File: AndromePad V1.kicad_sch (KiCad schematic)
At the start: 0 parts

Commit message: finished default hackpad tutorial
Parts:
- added D1, D2: SK6812MINI, LED_SMD:LED_SK6812MINI_PLCC4_3.5x3.5mm_P1.75mm, symbol LED:SK6812MINI
- added SW1, SW2, SW3, SW4: SW_Push, Button_Switch_Keyboard:SW_Cherry_MX_1.00u_PCB, symbol Switch:SW_Push
- added U1: XIAO-RP2040-DIP, OPL_Footprints:XIAO-RP2040-DIP, symbol OPL:XIAO-RP2040-DIP
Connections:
- new net: D1.3 (DIN), U1.5 (GPIO6/SDA)
- new net: D1.1 (DOUT), D2.3 (DIN)
- new net +5V: D1.4 (VDD), D2.4 (VDD), U1.14 (VBUS)
- new net GND: D1.2 (VSS), D2.2 (VSS), SW1.1, SW2.1, SW3.1, SW4.1, U1.13 (GND)
- new net Pin 10: SW3.2, U1.10 (GPIO4/MISO)
- new net Pin 11: SW1.2, U1.11 (GPIO3/MOSI)
- new net Pin 8: SW4.2, U1.8 (GPIO1/RX)
- new net Pin 9: SW2.2, U1.9 (GPIO2/SCK)
- no-connect marks 0 -> 8
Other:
- company: (none) -> DwayneR Engineering
- title: (none) -> Andromepad V1

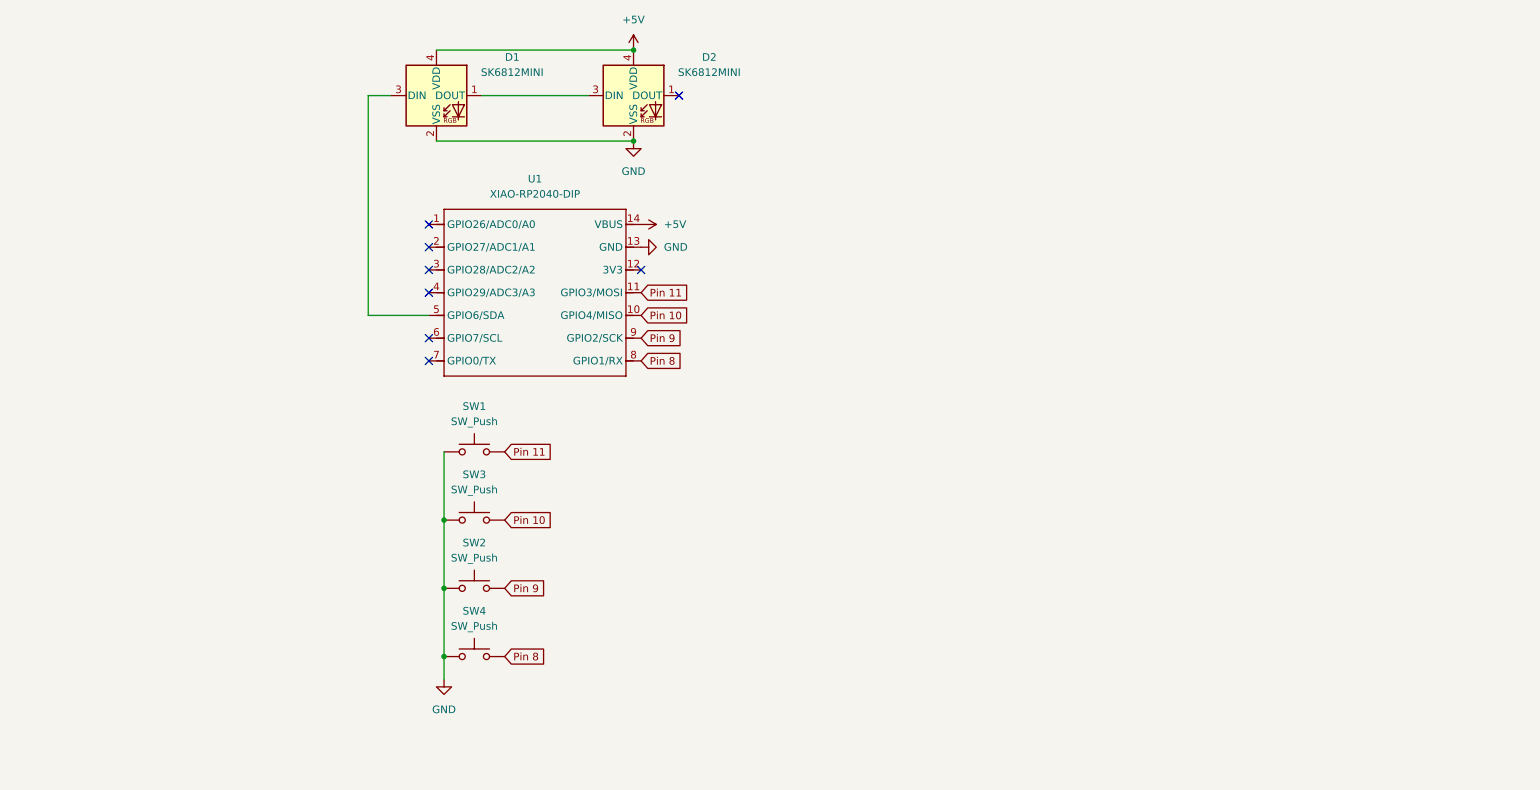
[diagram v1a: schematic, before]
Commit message: completed schematic, still have to work out errors and assign proper footprints
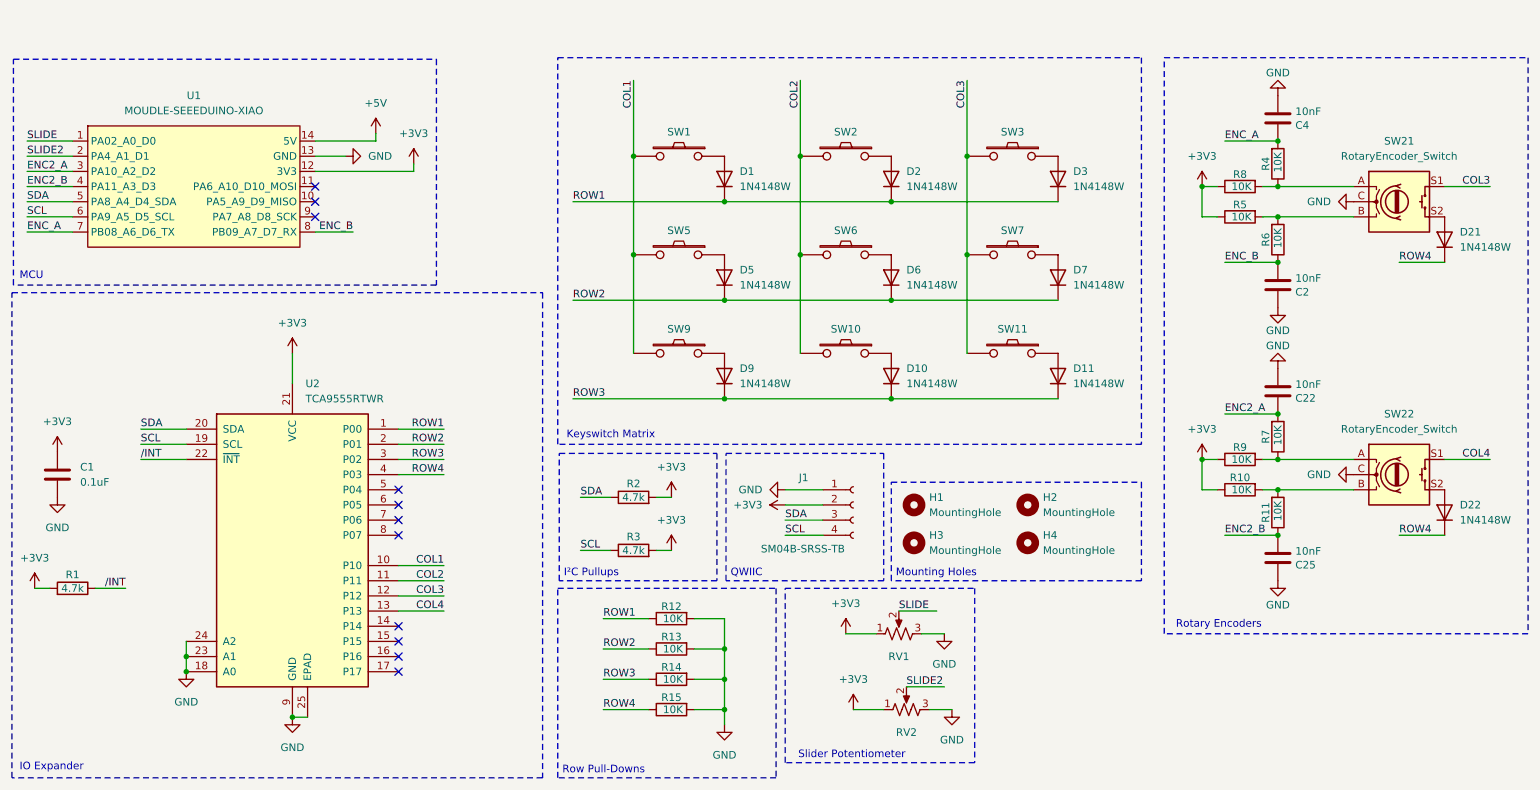
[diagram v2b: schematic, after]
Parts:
- removed D1, D2: SK6812MINI, LED_SMD:LED_SK6812MINI_PLCC4_3.5x3.5mm_P1.75mm, symbol LED:SK6812MINI
- removed SW1, SW2, SW3, SW4: SW_Push, Button_Switch_Keyboard:SW_Cherry_MX_1.00u_PCB, symbol Switch:SW_Push
- removed U1: XIAO-RP2040-DIP, OPL_Footprints:XIAO-RP2040-DIP, symbol OPL:XIAO-RP2040-DIP
- added C1: 0.1uF, Capacitor_SMD:C_0603_1608Metric_Pad1.08x0.95mm_HandSolder, symbol Device:C
- added C2, C22, C25, C4: 10nF, Capacitor_SMD:C_0603_1608Metric_Pad1.08x0.95mm_HandSolder, symbol Device:C
- added D1, D10, D11, D2, D21, D22, D3, D5, D6, D7, D9: 1N4148W, Diode_SMD:D_SOD-123, symbol Device:D
- added H1, H2, H3, H4: MountingHole, MountingHole:MountingHole_2.2mm_M2, symbol Mechanical:MountingHole
- added J1: SM04B-SRSS-TB, zzz_Project:CONN_SM04B-SRSS-TB_JST, symbol Connector:Conn_01x04_Socket
- added R1, R2, R3: 4.7k, Resistor_SMD:R_0603_1608Metric_Pad0.98x0.95mm_HandSolder, symbol Device:R
- added R10, R11, R12, R13, R14, R15, R4, R5, R6, R7, R8, R9: 10K, Resistor_SMD:R_0603_1608Metric_Pad0.98x0.95mm_HandSolder, symbol Device:R
- added RV1, RV2: R_Potentiometer_US, zzz_Project:PTA6043-2010CIB103, symbol Device:R_Potentiometer_US
- added SW1, SW10, SW11, SW2, SW3, SW5, SW6, SW7, SW9: keyswitch, Button_Switch_Keyboard:SW_Cherry_MX_1.00u_PCB, symbol Ians_symbols:keyswitch
- added SW21, SW22: RotaryEncoder_Switch, Rotary_Encoder:RotaryEncoder_Alps_EC11E-Switch_Vertical_H20mm, symbol Device:RotaryEncoder_Switch
- added U1: MOUDLE-SEEEDUINO-XIAO, OPL_Footprints:XIAO-RP2040-SMD, symbol MOUDLE-SEEEDUINO-XIAO:MOUDLE-SEEEDUINO-XIAO
- added U2: TCA9555RTWR, Package_DFN_QFN:WQFN-24-1EP_4x4mm_P0.5mm_EP2.45x2.45mm, symbol Interface_Expansion:TCA9555RTWR
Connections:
- net +5V: now also U1.14 (5V)
- net GND: now also C1.2, C2.2, C22.1, C25.2, C4.1, J1.1 (Pin_1), R12.2, R13.2, R14.2, R15.2, RV1.3, RV2.3, SW21.C, SW22.C, U1.13 (GND), U2.18 (A0), U2.23 (A1), U2.24 (A2), U2.25 (EPAD), U2.9 (GND)
- new net: R4.1, R8.2, SW21.A
- new net: D5.2 (A), SW5.1
- new net: D6.2 (A), SW6.1
- new net: D7.2 (A), SW7.1
- new net: D22.2 (A), SW22.S2
- new net: R7.1, R9.2, SW22.A
- new net: R10.2, R11.2, SW22.B
- new net: D3.2 (A), SW3.1
- new net: D11.2 (A), SW11.1
- new net: R5.2, R6.2, SW21.B
- new net: D21.2 (A), SW21.S2
- new net: D2.2 (A), SW2.1
- new net: D10.2 (A), SW10.1
- new net: D9.2 (A), SW9.1
- new net: D1.2 (A), SW1.1
- new net +3V3: C1.1, J1.2 (Pin_2), R1.2, R10.1, R2.2, R3.2, R5.1, R8.1, R9.1, RV1.1, RV2.1, U1.12 (3V3), U2.21 (VCC)
- new net COL1: SW1.2, SW5.2, SW9.2, U2.10 (P10)
- new net COL2: SW10.2, SW2.2, SW6.2, U2.11 (P11)
- new net COL3: SW11.2, SW21.S1, SW3.2, SW7.2, U2.12 (P12)
- new net COL4: SW22.S1, U2.13 (P13)
- new net ENC2_A: C22.2, R7.2, U1.3 (PA10_A2_D2)
- new net ENC2_B: C25.1, R11.1, U1.4 (PA11_A3_D3)
- new net ENC_A: C4.2, R4.2, U1.7 (PB08_A6_D6_TX)
- new net ENC_B: C2.1, R6.1, U1.8 (PB09_A7_D7_RX)
- new net ROW1: D1.1 (K), D2.1 (K), D3.1 (K), R12.1, U2.1 (P00)
- new net ROW2: D5.1 (K), D6.1 (K), D7.1 (K), R13.1, U2.2 (P01)
- new net ROW3: D10.1 (K), D11.1 (K), D9.1 (K), R14.1, U2.3 (P02)
- new net ROW4: D21.1 (K), D22.1 (K), R15.1, U2.4 (P03)
- new net SCL: J1.4 (Pin_4), R3.1, U1.6 (PA9_A5_D5_SCL), U2.19 (SCL)
- new net SDA: J1.3 (Pin_3), R2.1, U1.5 (PA8_A4_D4_SDA), U2.20 (SDA)
- new net SLIDE: RV1.2, U1.1 (PA02_A0_D0)
- new net SLIDE2: RV2.2, U1.2 (PA4_A1_D1)
- new net /INT: R1.1, U2.22 (~{INT})
- no-connect marks 8 -> 11
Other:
- note added: "IO Expander"
- note added: "I²C Pullups"
- note added: "Keyswitch Matrix"
- note added: "MCU"
- note added: "Mounting Holes"
- note added: "QWIIC"
- note added: "Rotary Encoders"
- note added: "Row Pull-Downs"
- note added: "Slider Potentiometer"

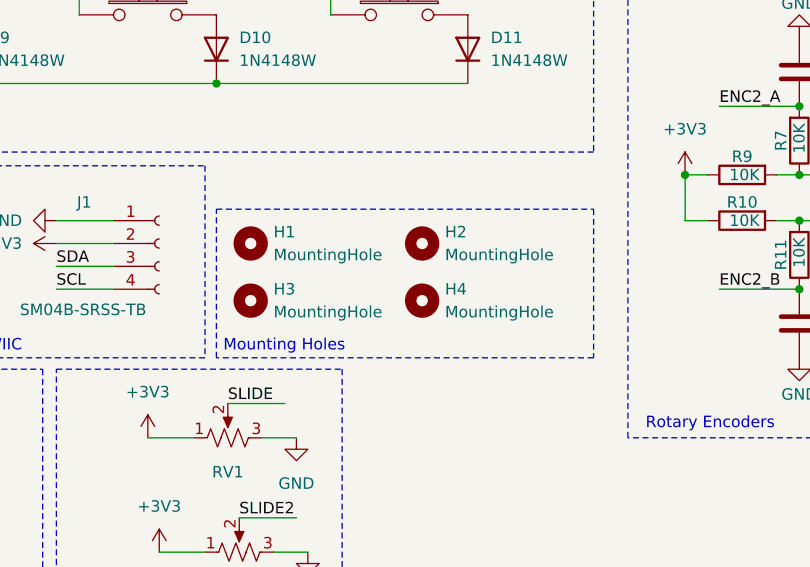
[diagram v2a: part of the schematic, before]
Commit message: finished routing in the pcb editor
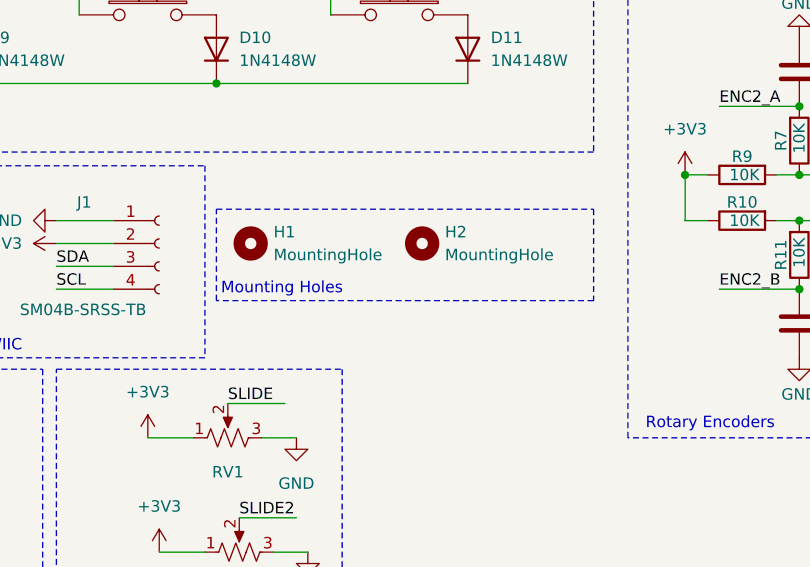
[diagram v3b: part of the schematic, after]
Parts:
- removed H3, H4: MountingHole, MountingHole:MountingHole_2.2mm_M2, symbol Mechanical:MountingHole
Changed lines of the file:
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@@
 	(rectangle
 		(start 167.64 110.49)
-		(end 209.55 127)
+		(end 209.55 120.65)
 		(stroke
 			(width 0)
@@
 	(text "Mounting Holes"
 		(exclude_from_sim no)
-		(at 168.402 125.73 0)
+		(at 168.148 119.38 0)
 		(effects
 			(font
@@
 	)
 	(symbol
-		(lib_id "Mechanical:MountingHole")
-		(at 190.5 120.65 0)
-		(unit 1)
-		(exclude_from_sim yes)
-		(in_bom no)
-		(on_board yes)
-		(dnp no)
-		(fields_autoplaced yes)
-		(property "Reference" "H4"
-			(at 193.04 119.3799 0)
-			(effects
-				(font
-					(size 1.27 1.27)
-				)
-				(justify left)
-			)
-		)
-		(property "Value" "MountingHole"
-			(at 193.04 121.9199 0)
-			(effects
-				(font
-					(size 1.27 1.27)
-				)
-				(justify left)
-			)
-		)
-		(property "Footprint" "MountingHole:MountingHole_2.2mm_M2"
-			(at 190.5 120.65 0)
-			(effects
-				(font
-					(size 1.27 1.27)
-				)
-				(hide yes)
-			)
-		)
-		(property "Datasheet" "~"
-			(at 190.5 120.65 0)
-			(effects
-				(font
-					(size 1.27 1.27)
-				)
-				(hide yes)
-			)
-		)
-		(property "Description" "Mounting Hole without connection"
-			(at 190.5 120.65 0)
-			(effects
-				(font
-					(size 1.27 1.27)
-				)
-				(hide yes)
-			)
-		)
-		(property "DigiKey Part Number " ""
-			(at 190.5 120.65 0)
-			(effects
-				(font
-					(size 1.27 1.27)
-				)
-				(hide yes)
-			)
-		)
-		(property "DigiKey PartNumber" ""
-			(at 190.5 120.65 0)
-			(effects
-				(font
-					(size 1.27 1.27)
-				)
-				(hide yes)
-			)
-		)
-		(property "Part Number" ""
-			(at 190.5 120.65 0)
-			(effects
-				(font
-					(size 1.27 1.27)
-				)
-				(hide yes)
-			)
-		)
-		(instances
-			(project "AndromePad V1"
-				(path "/73e2afde-7fd9-4f29-99d5-d984596564ad"
-					(reference "H4")
-					(unit 1)
-				)
-			)
-		)
-	)
-	(symbol
 		(lib_id "Device:C")
 		(at 232.41 123.19 0)
@@
 					(unit 1)
 				)
-			)
-		)
-	)
-	(symbol
-		(lib_id "Mechanical:MountingHole")
-		(at 171.45 120.65 0)
-		(unit 1)
-		(exclude_from_sim yes)
-		(in_bom no)
-		(on_board yes)
-		(dnp no)
-		(fields_autoplaced yes)
-		(property "Reference" "H3"
-			(at 173.99 119.3799 0)
-			(effects
-				(font
-					(size 1.27 1.27)
-				)
-				(justify left)
-			)
-		)
-		(property "Value" "MountingHole"
-			(at 173.99 121.9199 0)
-			(effects
-				(font
-					(size 1.27 1.27)
-				)
-				(justify left)
-			)
-		)
-		(property "Footprint" "MountingHole:MountingHole_2.2mm_M2"
-			(at 171.45 120.65 0)
-			(effects
-				(font
-					(size 1.27 1.27)
-				)
-				(hide yes)
-			)
-		)
-		(property "Datasheet" "~"
-			(at 171.45 120.65 0)
-			(effects
-				(font
-					(size 1.27 1.27)
-				)
-				(hide yes)
-			)
-		)
-		(property "Description" "Mounting Hole without connection"
-			(at 171.45 120.65 0)
-			(effects
-				(font
-					(size 1.27 1.27)
-				)
-				(hide yes)
-			)
-		)
-		(property "DigiKey Part Number " ""
-			(at 171.45 120.65 0)
-			(effects
-				(font
-					(size 1.27 1.27)
-				)
-				(hide yes)
-			)
-		)
-		(property "DigiKey PartNumber" ""
-			(at 171.45 120.65 0)
-			(effects
-				(font
-					(size 1.27 1.27)
-				)
-				(hide yes)
-			)
-		)
-		(property "Part Number" ""
-			(at 171.45 120.65 0)
-			(effects
-				(font
-					(size 1.27 1.27)
-				)
-				(hide yes)
-			)
-		)
-		(instances
-			(project "AndromePad V1"
-				(path "/73e2afde-7fd9-4f29-99d5-d984596564ad"
-					(reference "H3")
-					(unit 1)
-				)

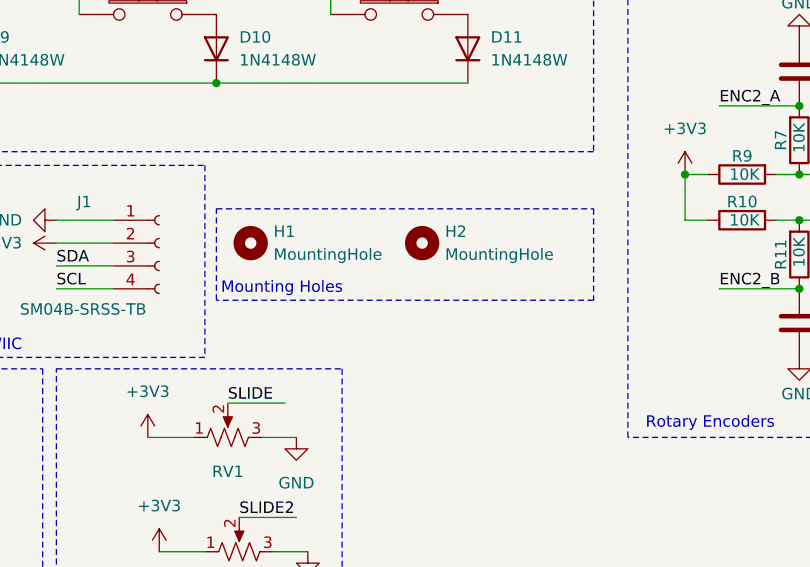
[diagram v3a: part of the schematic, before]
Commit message: feat: updated layout in pcb editor (much cleaner layout and better routing than before)
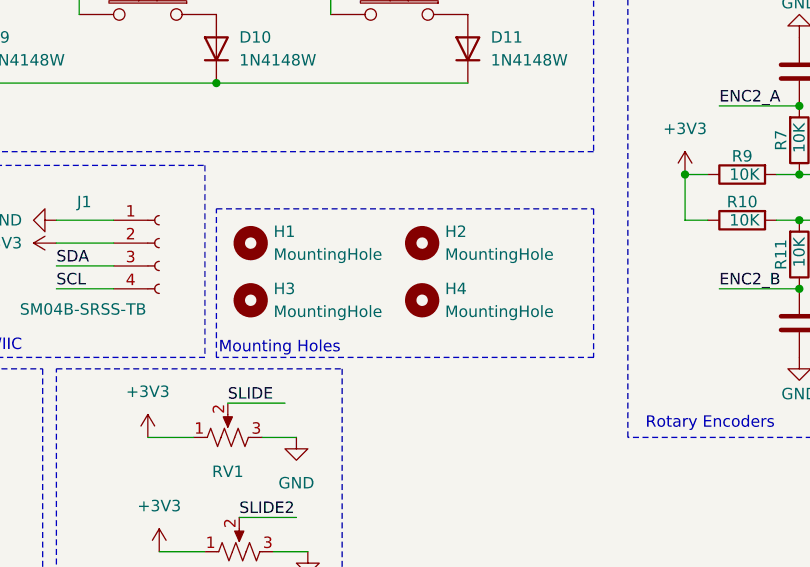
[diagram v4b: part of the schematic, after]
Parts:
- added H3, H4: MountingHole, MountingHole:MountingHole_2.2mm_M2, symbol Mechanical:MountingHole
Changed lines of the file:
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@@
 	(rectangle
 		(start 167.64 110.49)
-		(end 209.55 120.65)
+		(end 209.55 127)
 		(stroke
 			(width 0)
@@
 	(text "Mounting Holes"
 		(exclude_from_sim no)
-		(at 168.148 119.38 0)
+		(at 167.894 125.984 0)
 		(effects
 			(font
@@
 	)
 	(symbol
+		(lib_id "Mechanical:MountingHole")
+		(at 190.5 120.65 0)
+		(unit 1)
+		(exclude_from_sim yes)
+		(in_bom no)
+		(on_board yes)
+		(dnp no)
+		(fields_autoplaced yes)
+		(property "Reference" "H4"
+			(at 193.04 119.3799 0)
+			(effects
+				(font
+					(size 1.27 1.27)
+				)
+				(justify left)
+			)
+		)
+		(property "Value" "MountingHole"
+			(at 193.04 121.9199 0)
+			(effects
+				(font
+					(size 1.27 1.27)
+				)
+				(justify left)
+			)
+		)
+		(property "Footprint" "MountingHole:MountingHole_2.2mm_M2"
+			(at 190.5 120.65 0)
+			(effects
+				(font
+					(size 1.27 1.27)
+				)
+				(hide yes)
+			)
+		)
+		(property "Datasheet" "~"
+			(at 190.5 120.65 0)
+			(effects
+				(font
+					(size 1.27 1.27)
+				)
+				(hide yes)
+			)
+		)
+		(property "Description" "Mounting Hole without connection"
+			(at 190.5 120.65 0)
+			(effects
+				(font
+					(size 1.27 1.27)
+				)
+				(hide yes)
+			)
+		)
+		(property "DigiKey Part Number " ""
+			(at 190.5 120.65 0)
+			(effects
+				(font
+					(size 1.27 1.27)
+				)
+				(hide yes)
+			)
+		)
+		(property "DigiKey PartNumber" ""
+			(at 190.5 120.65 0)
+			(effects
+				(font
+					(size 1.27 1.27)
+				)
+				(hide yes)
+			)
+		)
+		(property "Part Number" ""
+			(at 190.5 120.65 0)
+			(effects
+				(font
+					(size 1.27 1.27)
+				)
+				(hide yes)
+			)
+		)
+		(instances
+			(project "AndromePad V1"
+				(path "/73e2afde-7fd9-4f29-99d5-d984596564ad"
+					(reference "H4")
+					(unit 1)
+				)
+			)
+		)
+	)
+	(symbol
 		(lib_id "Connector:Conn_01x04_Socket")
 		(at 161.29 114.3 0)
@@
 					(unit 1)
 				)
+			)
+		)
+	)
+	(symbol
+		(lib_id "Mechanical:MountingHole")
+		(at 171.45 120.65 0)
+		(unit 1)
+		(exclude_from_sim yes)
+		(in_bom no)
+		(on_board yes)
+		(dnp no)
+		(fields_autoplaced yes)
+		(property "Reference" "H3"
+			(at 173.99 119.3799 0)
+			(effects
+				(font
+					(size 1.27 1.27)
+				)
+				(justify left)
+			)
+		)
+		(property "Value" "MountingHole"
+			(at 173.99 121.9199 0)
+			(effects
+				(font
+					(size 1.27 1.27)
+				)
+				(justify left)
+			)
+		)
+		(property "Footprint" "MountingHole:MountingHole_2.2mm_M2"
+			(at 171.45 120.65 0)
+			(effects
+				(font
+					(size 1.27 1.27)
+				)
+				(hide yes)
+			)
+		)
+		(property "Datasheet" "~"
+			(at 171.45 120.65 0)
+			(effects
+				(font
+					(size 1.27 1.27)
+				)
+				(hide yes)
+			)
+		)
+		(property "Description" "Mounting Hole without connection"
+			(at 171.45 120.65 0)
+			(effects
+				(font
+					(size 1.27 1.27)
+				)
+				(hide yes)
+			)
+		)
+		(property "DigiKey Part Number " ""
+			(at 171.45 120.65 0)
+			(effects
+				(font
+					(size 1.27 1.27)
+				)
+				(hide yes)
+			)
+		)
+		(property "DigiKey PartNumber" ""
+			(at 171.45 120.65 0)
+			(effects
+				(font
+					(size 1.27 1.27)
+				)
+				(hide yes)
+			)
+		)
+		(property "Part Number" ""
+			(at 171.45 120.65 0)
+			(effects
+				(font
+					(size 1.27 1.27)
+				)
+				(hide yes)
+			)
+		)
+		(instances
+			(project "AndromePad V1"
+				(path "/73e2afde-7fd9-4f29-99d5-d984596564ad"
+					(reference "H3")
+					(unit 1)
+				)

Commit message: feat: added 3d models to footprints in kicad
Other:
- title: Andromepad V1 -> Andromepad V2
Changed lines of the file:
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@@
 	(paper "A4")
 	(title_block
-		(title "Andromepad V1")
+		(title "Andromepad V2")
 		(date "2025-12-04")
 		(rev "Version 1")
